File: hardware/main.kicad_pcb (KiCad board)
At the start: 2 copper layers, 50.5 x 28 mm, 40 parts, among them J1 2.54-1*5P, J2 KH-2.54FH-1X2P-H8.5, U1 74HC595, U2 74HC595

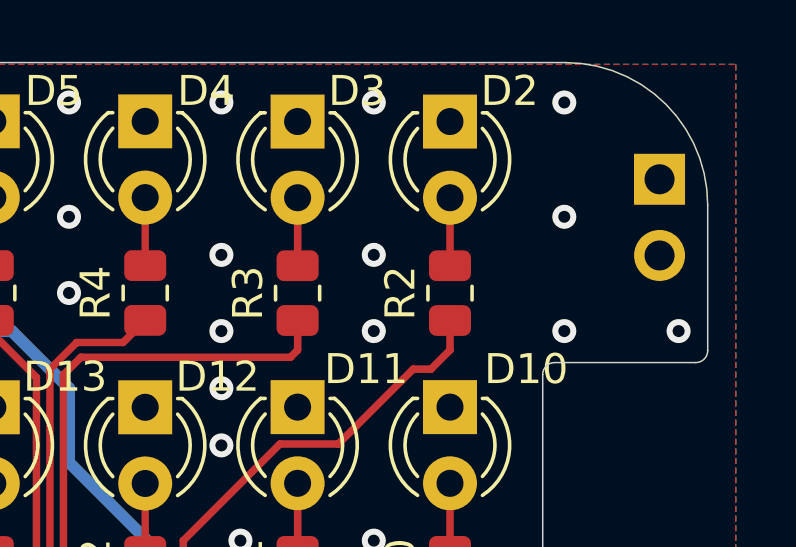
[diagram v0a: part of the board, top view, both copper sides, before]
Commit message: destroy pcb; fix sch
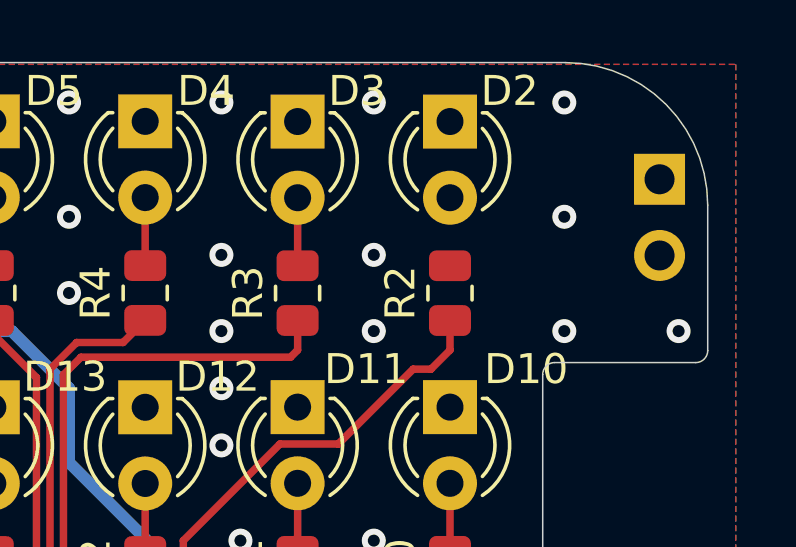
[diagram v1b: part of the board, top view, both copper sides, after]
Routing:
- net Net-(D2-A): track 2.27 -> 0.00 mm

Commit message: fix pcb
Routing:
- net Net-(D2-A): track 0.00 -> 2.27 mm
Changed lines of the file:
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@@
+	)
+	(segment
+		(start 70.91 35.7725)
+		(end 70.91 33.505)
+		(width 0.25)
+		(layer "F.Cu")
+		(net 4)
 	)
 	(segment
